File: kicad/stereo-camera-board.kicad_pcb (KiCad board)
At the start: 4 copper layers, 57 x 70 mm, 86 parts, among them IC1 ZLDO1117G33TA, IC2 MCP1700T-2502E/TT, IC3 SN74LVC1T45DCKR, IC4 SN74LVC1T45DCKR, IC5 SN74LVC1T45DCKR, P1 FSM4JSMA-SMD, T1 2n2222a, T2 2N2907A, U1 GSB311231HR, U2 ATXMEGA256A3-AU, U3 MAX3207E, U4 MPU-9250

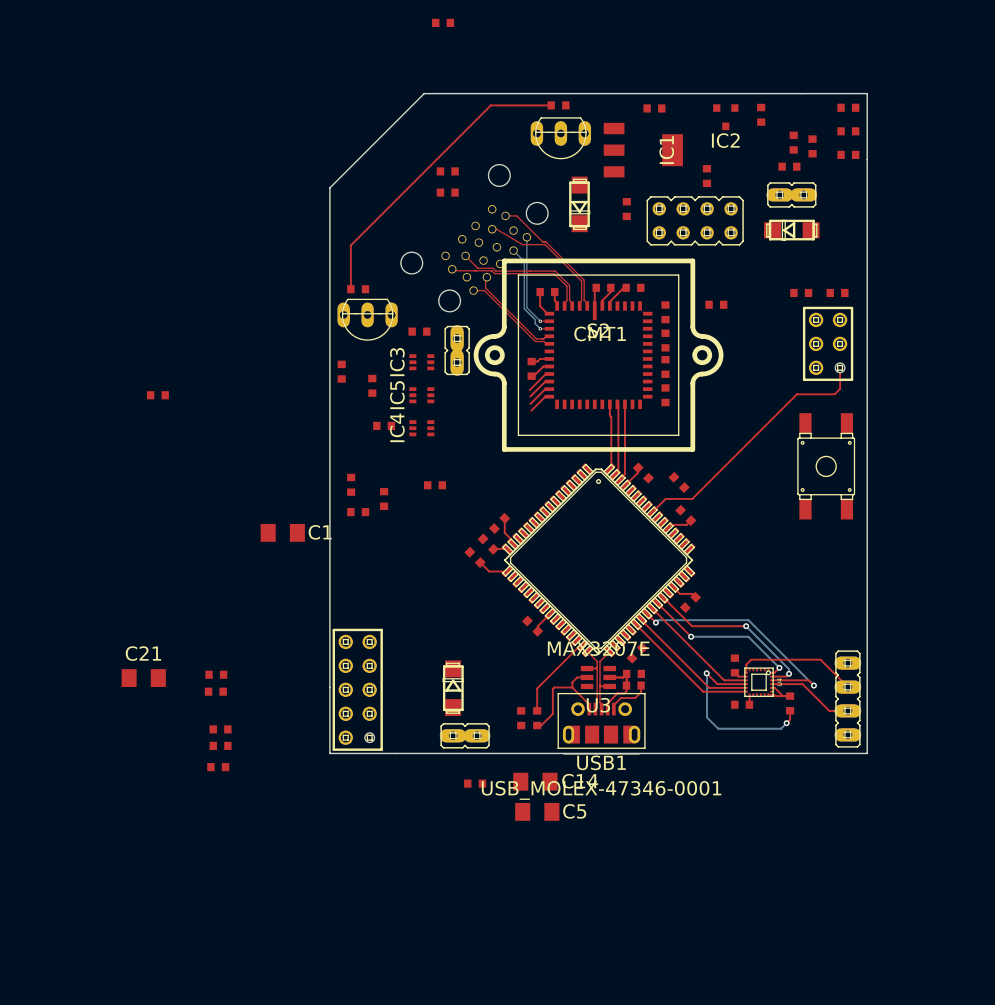
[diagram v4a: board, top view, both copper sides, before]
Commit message: Fixed power nets Fixed leds
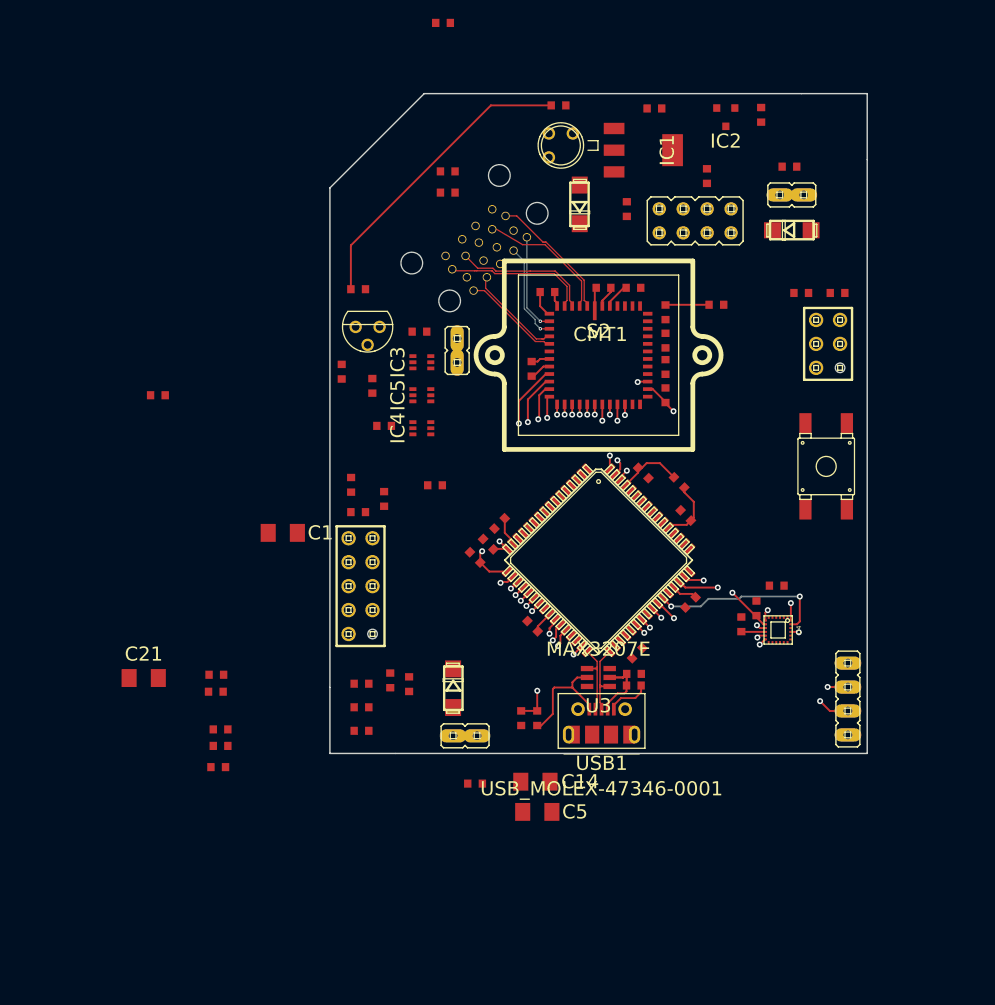
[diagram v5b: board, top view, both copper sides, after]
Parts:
- T1: footprint transistor-TO92-EBC -> transistor-TO92
- T2: footprint transistor-TO92-EBC -> transistor-TO18
- moved L1 80.0 mm to (123.3, 142.6)
- moved L2 80.0 mm to (123.3, 145.1)
- moved L3 80.0 mm to (123.3, 147.6)
- moved R11 71.3 mm to (128.4, 142.7)
- moved R12 71.3 mm to (126.4, 142.2)
- moved C26 13.2 mm to (167.4, 132.2)
- moved JP3 11.0 mm to (123.2, 132.2)
- moved C28 9.86 mm to (163.7, 136.3)
- moved C27 6.48 mm to (165.2, 134.6)
- moved U4 5.90 mm to (167.6, 136.9)
- turned FB1 to 0 degrees
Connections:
- C10 pad 2: N-00000119 -> GND
- C11 pad 2: N-0000088 (its old number) -> GND
- C12 pad 2: N-00000119 -> GND
- C13 pad 1: N-0000067 (its old number) -> +2.5V
- C15 pad 1: N-0000067 (its old number) -> +2.5V
- C16 pad 2: N-00000107 (its old number) -> GND
- C17 pad 2: N-00000107 (its old number) -> GND
- C18 pad 2: N-00000107 (its old number) -> GND
- C19 pad 2: N-00000107 (its old number) -> GND
- C2 pad 2: N-00000119 -> GND
- C20 pad 2: N-00000107 (its old number) -> GND
- C22 pad 1: N-0000068 (its old number) -> +3.3V
- C23 pad 2: N-00000120 -> GND
- C24 pad 1: N-0000068 (its old number) -> +3.3V
- C25 pad 1: N-0000090 (its old number) -> +3.3V
- C25 pad 2: N-0000089 (its old number) -> GND
- C26 pad 1: N-0000034 (its old number) -> +3.3V
- C26 pad 2: N-0000035 (its old number) -> GND
- C27 pad 1: N-0000034 (its old number) -> +3.3V
- C27 pad 2: N-0000035 (its old number) -> GND
- C28 pad 1: N-00000147 -> GND
- C3 pad 2: N-00000119 -> GND
- C31 pad 1: N-0000084 (its old number) -> GND
- C4 pad 2: N-00000119 -> GND
- C6 pad 1: N-0000022 (its old number) -> +3.3V
- C6 pad 2: N-0000033 (its old number) -> GND
- C7 pad 1: N-0000029 (its old number) -> +2.5V
- C7 pad 2: N-0000033 (its old number) -> GND
- C8 pad 1: N-0000032 (its old number) -> +5V
- C8 pad 2: N-0000030 (its old number) -> GND
- C9 pad 2: N-00000119 -> GND
- D1 pad A: N-0000030 (its old number) -> GND
- D1 pad C: N-0000032 (its old number) -> +5V
- D2 pad A: N-00000132 -> N-0000062
- D3 pad C: N-0000075 (its old number) -> +5V
- EXT_SENSOR1 pad 1: N-00000118 -> +3.3V
- EXT_SENSOR1 pad 4: N-00000117 -> GND
- FB1 pad 2: N-00000104 -> +3.3V
- IC1 pad 1: N-0000033 (its old number) -> GND
- IC1 pad 2: N-0000022 (its old number) -> +3.3V
- IC1 pad 3: N-0000080 (its old number) -> +5V
- IC2 pad 1: N-0000033 (its old number) -> GND
- IC2 pad 2: N-0000029 (its old number) -> +2.5V
- IC2 pad 3: N-0000022 (its old number) -> +3.3V
- IC3 pad 1: N-0000068 (its old number) -> +3.3V
- IC3 pad 6: N-0000067 (its old number) -> +2.5V
- IC4 pad 1: N-0000068 (its old number) -> +3.3V
- IC4 pad 6: N-0000067 (its old number) -> +2.5V
- IC5 pad 1: N-0000068 (its old number) -> +3.3V
- IC5 pad 6: N-0000067 (its old number) -> +2.5V
- J1 pad 1: N-0000030 (its old number) -> GND
- J1 pad 2: N-0000032 (its old number) -> +5V
- JP1 pad 1: N-00000128 -> GND
- JP1 pad 5: N-00000128 -> GND
- JP1 pad 7: N-00000128 -> GND
- JP3 pad 10: N-0000060 (its old number) -> GND
- JP3 pad 2: N-0000060 (its old number) -> GND
- P1 pad P$2: N-0000052 (its old number) -> GND
- PDIJTAG1 pad 2: N-0000092 (its old number) -> +3.3V
- PDIJTAG1 pad 6: N-0000096 (its old number) -> GND
- R1 pad 1: N-0000097 (its old number) -> +3.3V
- R10 pad 1: N-0000083 (its old number) -> N-0000045
- R13 pad 1: N-000009 (its old number) -> GND
- R14 pad 1: N-0000086 (its old number) -> GND
- R17 pad 1: N-0000082 (its old number) -> GND
- R17 pad 2: N-0000083 (its old number) -> N-0000045
- R18 pad 1: N-0000081 (its old number) -> N-0000046
- R18 pad 2: N-00000143 -> N-00000109
- R19 pad 1: N-00000139 -> GND
- R2 pad 1: N-0000097 (its old number) -> +3.3V
- R2 pad 2: N-00000128 -> GND
- R20 pad 1: N-0000080 (its old number) -> +5V
- R20 pad 2: N-00000143 -> N-00000109
- R22 pad 2: N-0000067 (its old number) -> +2.5V
- R24 pad 2: N-0000084 (its old number) -> GND
- R25 pad 2: N-0000046 -> +3.3V
- R3 pad 1: N-0000026 (its old number) -> +3.3V
- R4 pad 1: N-0000026 (its old number) -> +3.3V
- R5 pad 1: N-00000119 -> GND
- R8 pad 2: N-0000067 (its old number) -> +2.5V
- R9 pad 2: N-0000067 (its old number) -> +2.5V
- S2 pad 12: N-00000119 -> GND
- S2 pad 13: N-00000119 -> GND
- S2 pad 29: N-00000119 -> GND
- S2 pad 30: N-00000119 -> GND
- S2 pad 31: N-00000119 -> GND
- S2 pad 34: N-00000119 -> GND
- S2 pad 38: N-00000119 -> GND
- S2 pad 48: N-00000119 -> GND
- S2 pad 7: N-00000119 -> GND
- U1 pad 13: N-0000043 (its old number) -> GND
- U2 pad 14: N-00000120 -> GND
- U2 pad 24: N-00000120 -> GND
- U2 pad 34: N-00000120 -> GND
- U2 pad 44: N-00000120 -> GND
- U2 pad 52: N-00000120 -> GND
- U2 pad 60: N-00000120 -> GND
- U4 pad 1: N-0000048 (its old number) -> +3.3V
- U4 pad 13: N-0000034 (its old number) -> +3.3V
- U4 pad 18: N-00000147 -> GND
- U4 pad 20: N-00000147 -> GND
- U4 pad 8: N-0000034 (its old number) -> +3.3V
- USB1 pad 5: N-0000084 (its old number) -> GND
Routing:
- net N-0000012: track 2.79 -> 45.0 mm, vias 0 -> 2
- net N-0000021: track 2.70 -> 42.5 mm, vias 0 -> 2
- net N-0000022: track 2.66 -> 40.1 mm, vias 0 -> 2
- net N-0000059: track 0.00 -> 35.0 mm, vias 0 -> 2
- net N-00000143: track 32.1 -> 0.00 mm
- net N-00000109: track 0.00 -> 32.1 mm
- net N-0000034: track 0.00 -> 31.7 mm, vias 0 -> 2
- net N-0000028: track 2.56 -> 34.0 mm, vias 0 -> 2
- net N-0000058: track 0.00 -> 30.8 mm, vias 0 -> 2
- net N-0000033: track 0.00 -> 30.2 mm, vias 0 -> 2
- net N-0000044: track 0.00 -> 28.8 mm, vias 0 -> 2
- net N-0000011: track 27.5 -> 0.00 mm
- net N-0000023: track 0.00 -> 26.3 mm, vias 0 -> 2
- net N-0000031: track 25.8 -> 0.05 mm, vias 2 -> 0
- net N-0000024: track 0.00 -> 24.8 mm, vias 0 -> 2
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- removed copper zone on Inner1.Cu, net (none)
- removed copper zone on Inner2.Cu, net (none)

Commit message: Saved Pcbnew with updated netlist
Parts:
- moved J1 30.1 mm to (139.6, 84.5), turned to 0 degrees
- moved R13 23.5 mm to (157.9, 146.6)
- moved D3 2.76 mm to (131.2, 145.2)
- moved JP6 1.70 mm to (135.9, 147.4)
- moved JP2 0.29 mm to (133.3, 107.5), turned to 180 degrees
- turned C25 to 180 degrees
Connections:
- B1 pad 1: (no net) -> +3.3V
- B1 pad 2: (no net) -> N-0000057
- C1 pad 1: (no net) -> +5V
- C1 pad 2: (no net) -> GND
- C14 pad 1: (no net) -> N-0000057
- C14 pad 2: (no net) -> GND
- C21 pad 1: (no net) -> N-0000081
- C21 pad 2: (no net) -> GND
- C23 pad 1: N-0000080 (its old number) -> N-0000081
- C5 pad 1: (no net) -> +3.3V
- C5 pad 2: (no net) -> GND
- FB2 pad 2: N-0000080 (its old number) -> N-0000081
- L1 pad 1: (no net) -> +3.3V
- L1 pad 2: (no net) -> N-0000020
- L2 pad 1: (no net) -> +3.3V
- L2 pad 2: (no net) -> N-0000019
- L3 pad 1: (no net) -> +3.3V
- L3 pad 2: (no net) -> N-0000018
- R11 pad 2: N-0000018 -> N-0000020
- R12 pad 2: N-0000017 (its old number) -> N-0000019
- R13 pad 2: N-0000016 (its old number) -> N-0000018
- U2 pad 61: N-0000080 (its old number) -> N-0000081
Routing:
- net N-0000081: track 0.00 -> 6.98 mm
- net N-0000080 (its old number): track 6.98 -> 0.00 mm

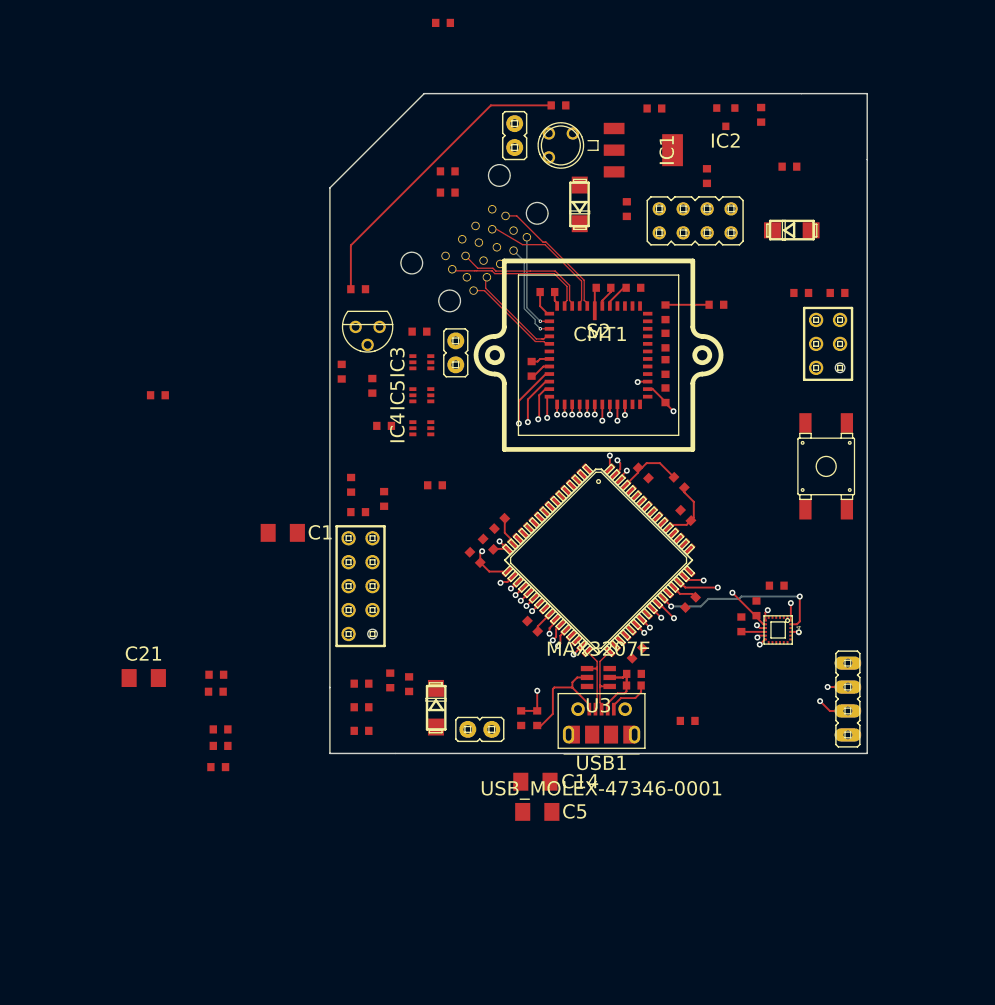
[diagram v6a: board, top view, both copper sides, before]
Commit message: Fixed pins on leds, capacitors, and sensor. Regenerated netlist Added thicker trace width to pcb
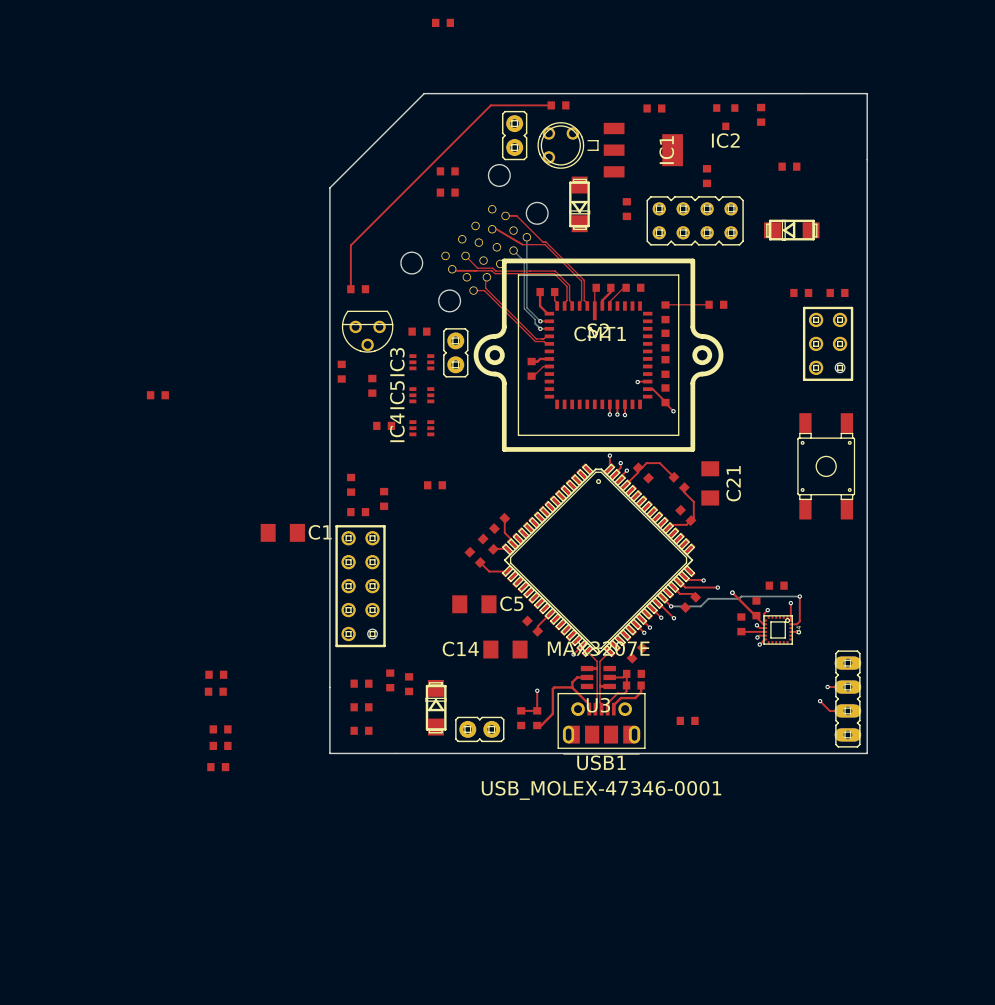
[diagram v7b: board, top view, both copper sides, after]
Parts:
- moved C21 63.5 mm to (160.3, 121.3), turned to 270 degrees
- moved C5 23.0 mm to (135.3, 134.2)
- moved C14 14.4 mm to (138.6, 139.0), turned to 180 degrees
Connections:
- C11 pad 1: N-0000077 (its old number) -> +3.3V
- C13 pad 2: N-0000073 -> GND
- C15 pad 2: N-0000073 -> GND
- C22 pad 2: N-0000073 -> GND
- C24 pad 2: N-0000073 -> GND
- C30 pad 2: N-00000105 (its old number) -> GND
- IC3 pad 2: N-0000073 -> GND
- IC4 pad 2: N-0000073 -> GND
- IC5 pad 2: N-0000073 -> GND
- R16 pad 2: N-00000105 (its old number) -> GND
- U1 pad 1: N-0000078 (its old number) -> +5V
- U1 pad 4: N-00000105 (its old number) -> GND
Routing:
- net N-0000029: track 45.0 -> 0.00 mm, vias 2 -> 0
- net N-000005: track 42.5 -> 0.00 mm, vias 2 -> 0
- net N-000006: track 40.1 -> 0.00 mm, vias 2 -> 0
- net N-0000027: track 34.0 -> 0.00 mm, vias 2 -> 0
- net N-0000031: track 31.7 -> 0.00 mm, vias 2 -> 0
- net N-0000032: track 30.2 -> 0.00 mm, vias 2 -> 0
- net N-0000041: track 28.8 -> 0.00 mm, vias 2 -> 0
- net N-0000022: track 26.3 -> 0.00 mm, vias 2 -> 0
- net N-0000023: track 24.8 -> 0.00 mm, vias 2 -> 0
- net N-0000071: track 25.4 -> 3.26 mm, vias 2 -> 0
- net N-0000068: track 21.3 -> 1.49 mm, vias 2 -> 0
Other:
- net class Default: clearance 0.1 -> 0.127; via_dia 0.635 -> 0.4572; via_drill 0.381 -> 0.254
- net class Thicker added: clearance 0.127, trace_width 0.254, via_dia 0.508, via_drill 0.254
- net class USB: clearance 0.1 -> 0.127
- rule trace_clearance: 0.1 -> 0.127

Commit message: Mirrored molex.mod (I'm not sure this is right, Kicad may do this on its own) Fixed square pin on jtag connectors
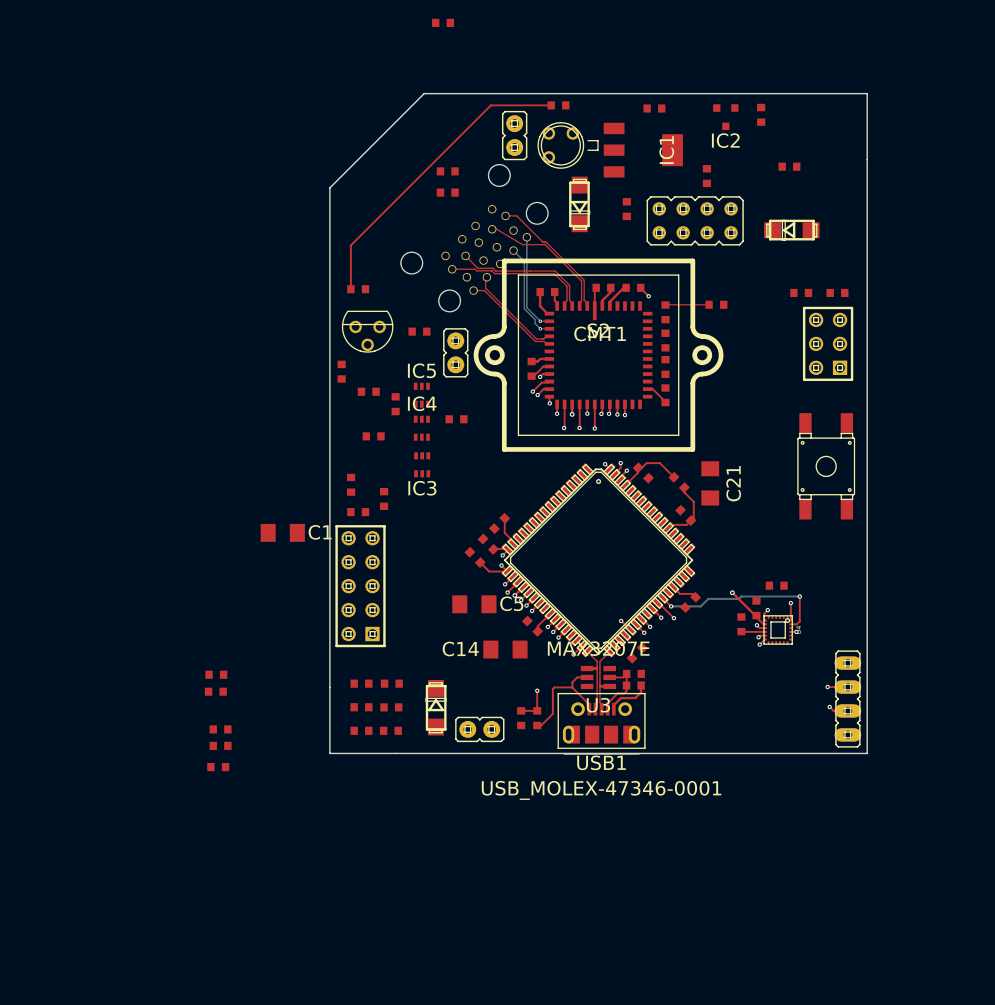
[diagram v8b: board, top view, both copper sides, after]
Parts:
- moved R13 31.5 mm to (126.5, 147.6), turned to 180 degrees
- moved B1 25.2 mm to (127.0, 113.0), turned to 270 degrees
- moved IC3 10.9 mm to (129.8, 119.4), turned to 180 degrees
- moved R7 7.36 mm to (133.4, 114.5)
- moved R12 2.86 mm to (126.5, 145.1), turned to 180 degrees
- moved R11 1.83 mm to (126.6, 142.6), turned to 180 degrees
- moved R8 1.57 mm to (124.6, 116.4)
- moved R10 0.74 mm to (124.1, 111.6), turned to 0 degrees
- turned IC4 to 0 degrees
- turned IC5 to 0 degrees
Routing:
- net N-0000029: track 0.00 -> 41.1 mm, vias 0 -> 2
- net N-0000047: track 0.00 -> 39.0 mm, vias 0 -> 2
- net N-000005: track 0.00 -> 38.7 mm, vias 0 -> 2
- net N-000006: track 0.00 -> 36.3 mm, vias 0 -> 2
- net N-0000057: track 35.0 -> 0.00 mm, vias 2 -> 0
- net N-0000027: track 0.00 -> 31.9 mm, vias 0 -> 2
- net N-0000031: track 0.00 -> 29.7 mm, vias 0 -> 2
- net N-0000032: track 0.00 -> 28.4 mm, vias 0 -> 2
- net N-000004: track 30.8 -> 2.52 mm, vias 2 -> 0
- net N-0000041: track 0.00 -> 27.1 mm, vias 0 -> 2
- net N-0000071: track 3.26 -> 29.5 mm, vias 0 -> 2
- net N-0000022: track 0.00 -> 25.6 mm, vias 0 -> 2
- net N-0000068: track 1.49 -> 26.0 mm, vias 0 -> 2
- net N-0000023: track 0.00 -> 23.8 mm, vias 0 -> 2
